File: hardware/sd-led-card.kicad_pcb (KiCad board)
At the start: 2 copper layers, 24 x 32 mm, 26 parts, among them J1 J1, U1 RP2350A

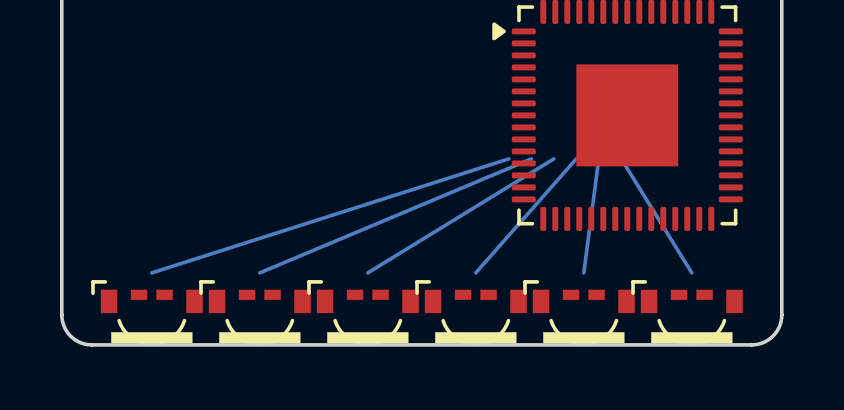
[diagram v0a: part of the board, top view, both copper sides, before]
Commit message: Move edge LEDs closer
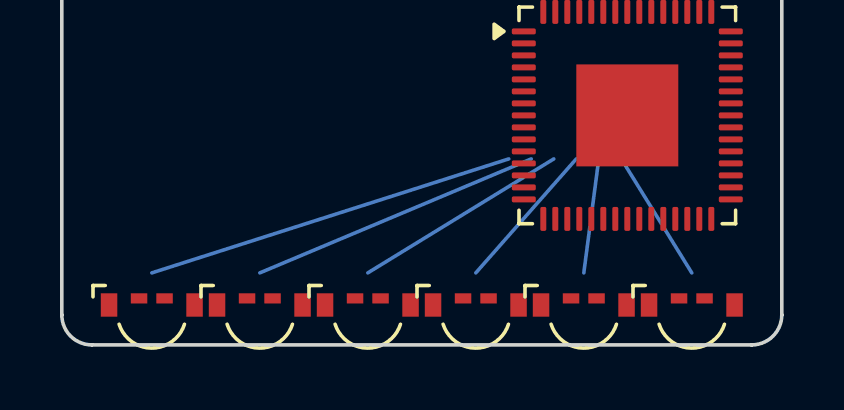
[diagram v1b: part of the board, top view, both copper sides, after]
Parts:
- removed the DBG at (0.00, 0.00) (x8)
- removed the J1 at (0.00, 0.00) (x9)
- added DBG (x8): DBG, , F.Cu at (0.00, 0.00)
- added J1 (x9): J1, , F.Cu at (0.00, 0.00)
- moved D1 0.12 mm to (41.0, 65.2)
- moved D2 0.12 mm to (44.6, 65.2)
- moved D3 0.12 mm to (48.2, 65.2)
- moved D4 0.12 mm to (51.8, 65.2)
- moved D5 0.12 mm to (55.4, 65.2)
- moved D6 0.12 mm to (59.0, 65.2)

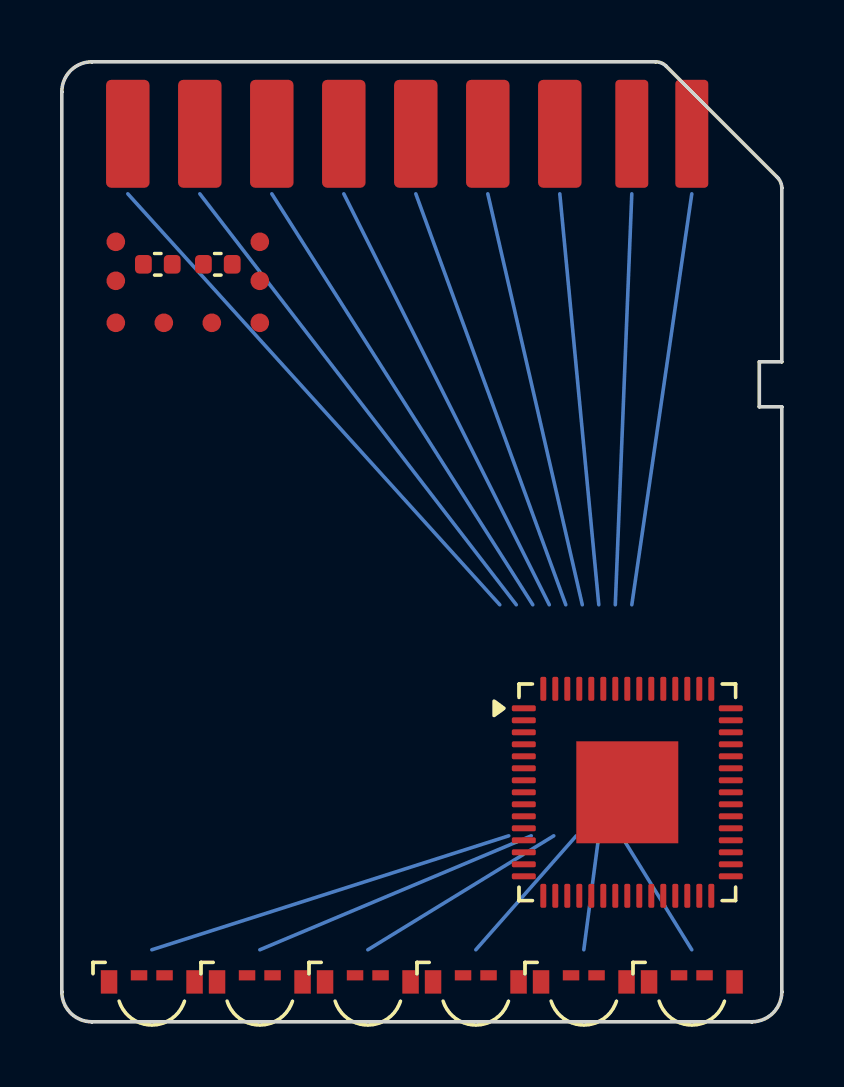
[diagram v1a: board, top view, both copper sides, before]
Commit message: Rebase layout on SD card footprint
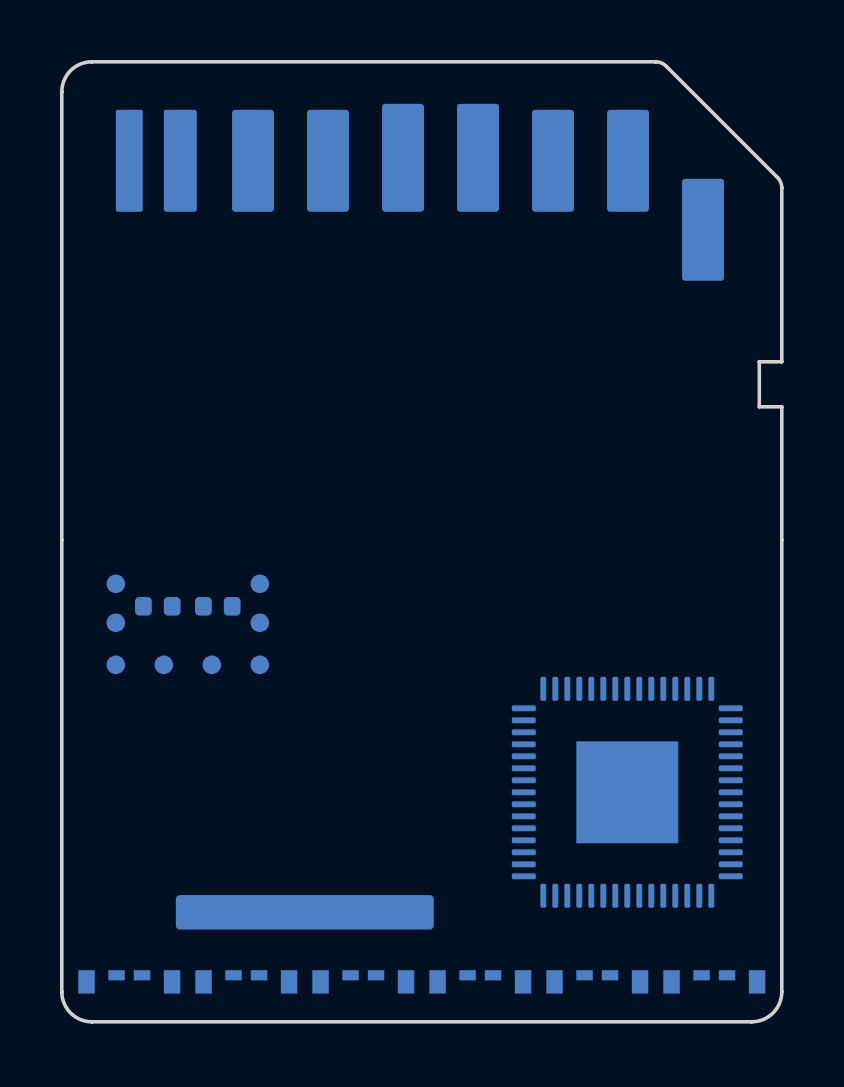
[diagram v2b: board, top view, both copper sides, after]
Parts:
- removed the DBG at (0.00, 0.00) (x8)
- removed the J1 at (0.00, 0.00) (x9)
- added CT1: CT1, , B.Cu at (0.00, 0.00)
- added DBG (x8): DBG, , B.Cu at (0.00, 0.00)
- added J1: SD card edge contacts, SD_Card_Device_16mm_SlotDepth, F.Cu at (50.0, 50.0)
- C1, C2, D1, D2, D3, D4, D5, D6, U1: moved to B.Cu
- moved C1 11.4 mm to (41.2, 52.1), turned to 180 degrees
- moved C2 11.4 mm to (43.2, 52.1), turned to 180 degrees
- moved D1 0.75 mm to (40.2, 65.2), turned to 180 degrees
- moved D6 0.75 mm to (59.8, 65.2), turned to 180 degrees
- moved D2 0.45 mm to (44.1, 65.2), turned to 180 degrees
- moved D5 0.45 mm to (55.9, 65.2), turned to 180 degrees
- moved D3 0.15 mm to (48.0, 65.2), turned to 180 degrees
- moved D4 0.15 mm to (52.0, 65.2), turned to 180 degrees
- turned U1 to 180 degrees
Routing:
- net (no net): track 180.2 -> 0.00 mm
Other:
- board size 24 x 32 mm -> 24 x 16 mm
